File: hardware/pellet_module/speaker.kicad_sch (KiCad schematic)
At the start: 10 parts, among them U3 TPA2005D1

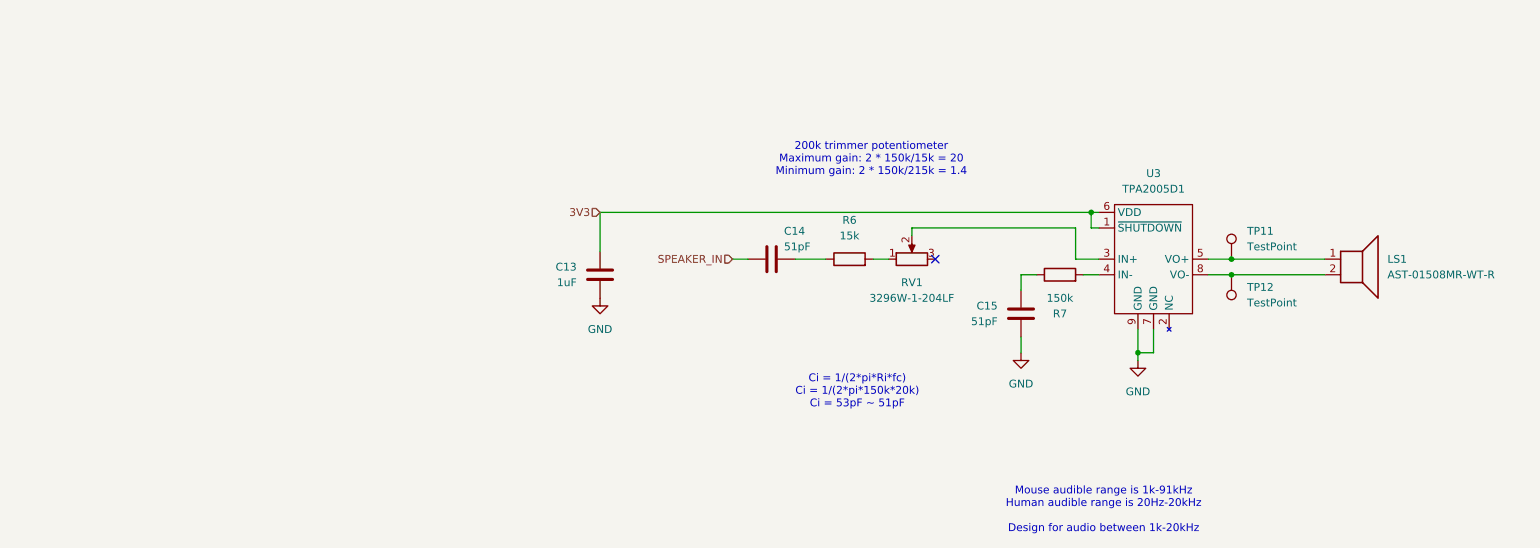
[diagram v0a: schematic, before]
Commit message: Make schematic changes for the following v1.1 changes: * Correct servo pinout * CAN IN / CAN OUT designation * Add pulldown to BOOT pin and pullup to nRST * Add volume control & shutdown capability to audio amplifier
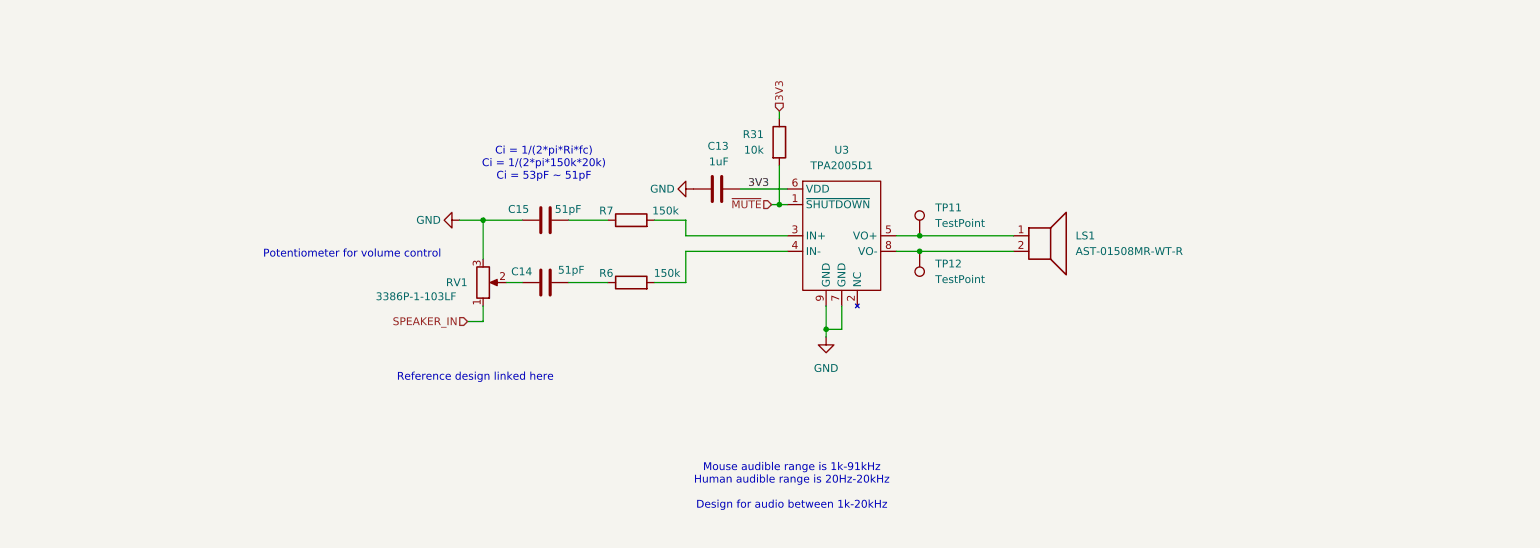
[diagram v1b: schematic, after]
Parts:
- added R31: 10k, Resistor_SMD:R_0603_1608Metric, symbol Device:R
- R6: value 15k -> 150k; LCSC C22809 -> C22807; MPN 0603WAF1502T5E -> 0603WAF1503T5E
- RV1: value 3296W-1-204LF -> 3386P-1-103LF; footprint Potentiometer_THT:Potentiometer_Bourns_3296W_Vertical -> Potentiometer_THT:Potentiometer_Bourns_3386P_Vertical; LCSC C58354 -> C116281; MPN 3296W-1-204LF -> 3386P-1-103LF
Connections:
- net 3V3: now also R31.1; no longer U3.1 (~{SHUTDOWN})
- net GND: now also C15.1, RV1.3; no longer C15.2
- net SPEAKER_IN: now also RV1.1; no longer C14.1
- net at R6.2: now also U3.4 (IN-); no longer RV1.1
- net at RV1.2: now also C14.1; no longer U3.3 (IN+)
- net at R7.1: now also C15.2; no longer C15.1
- net at R7.2: now also U3.3 (IN+); no longer U3.4 (IN-)
- new net ~{MUTE}: R31.2, U3.1 (~{SHUTDOWN})
- no-connect marks 1 -> 0
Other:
- note added: "Potentiometer for volume control"
- note added: "Reference design linked here"
- note removed: "200k trimmer potentiometer Maximum gain: 2 * 150k/15k = 20 Minimum gain: 2 * 150k/215k = 1.4"
- moved on the sheet: C13, C14, C15, LS1, R6, R7, RV1, TP11, TP12, U3

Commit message: add test points to schematic
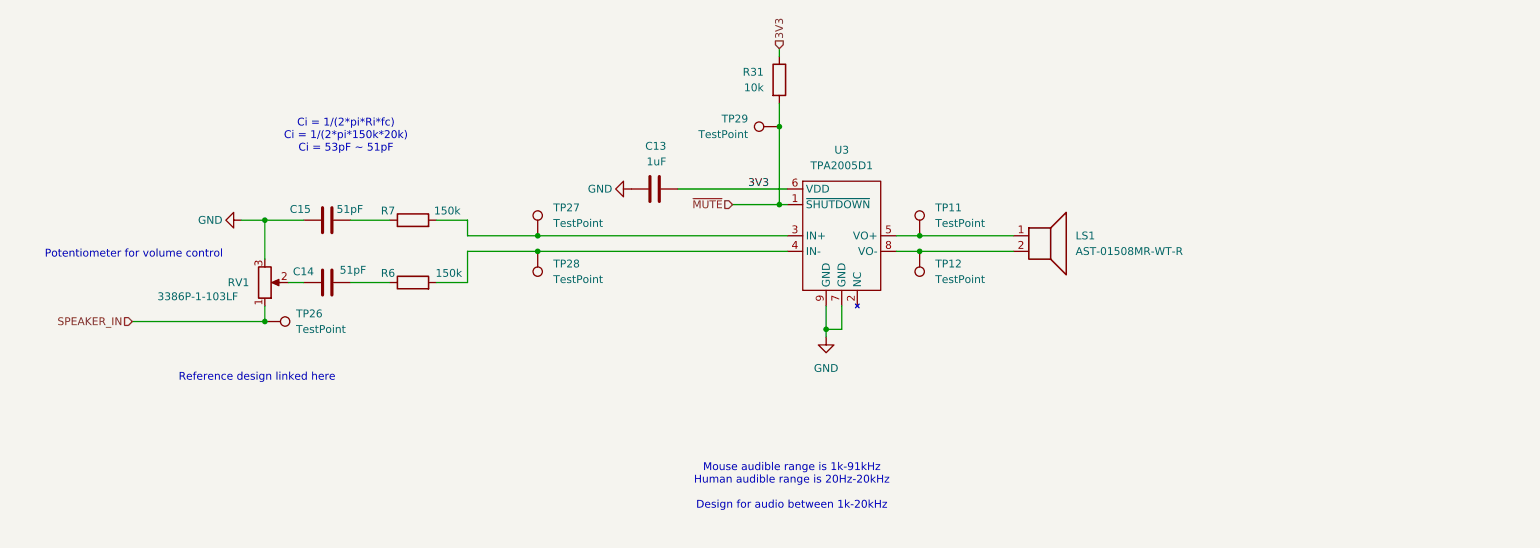
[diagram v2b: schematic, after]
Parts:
- added TP26, TP27, TP28, TP29: TestPoint, TestPoint:TestPoint_Pad_1.0x1.0mm, symbol Connector:TestPoint
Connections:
- net SPEAKER_IN: now also TP26.1
- net ~{MUTE}: now also TP29.1
- net at R6.2, U3.4 (IN-): now also TP28.1
- net at R7.2, U3.3 (IN+): now also TP27.1
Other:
- moved on the sheet: C13, C14, C15, R31, R6, R7, RV1
